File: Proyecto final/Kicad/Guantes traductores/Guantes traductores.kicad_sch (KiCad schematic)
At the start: 0 parts

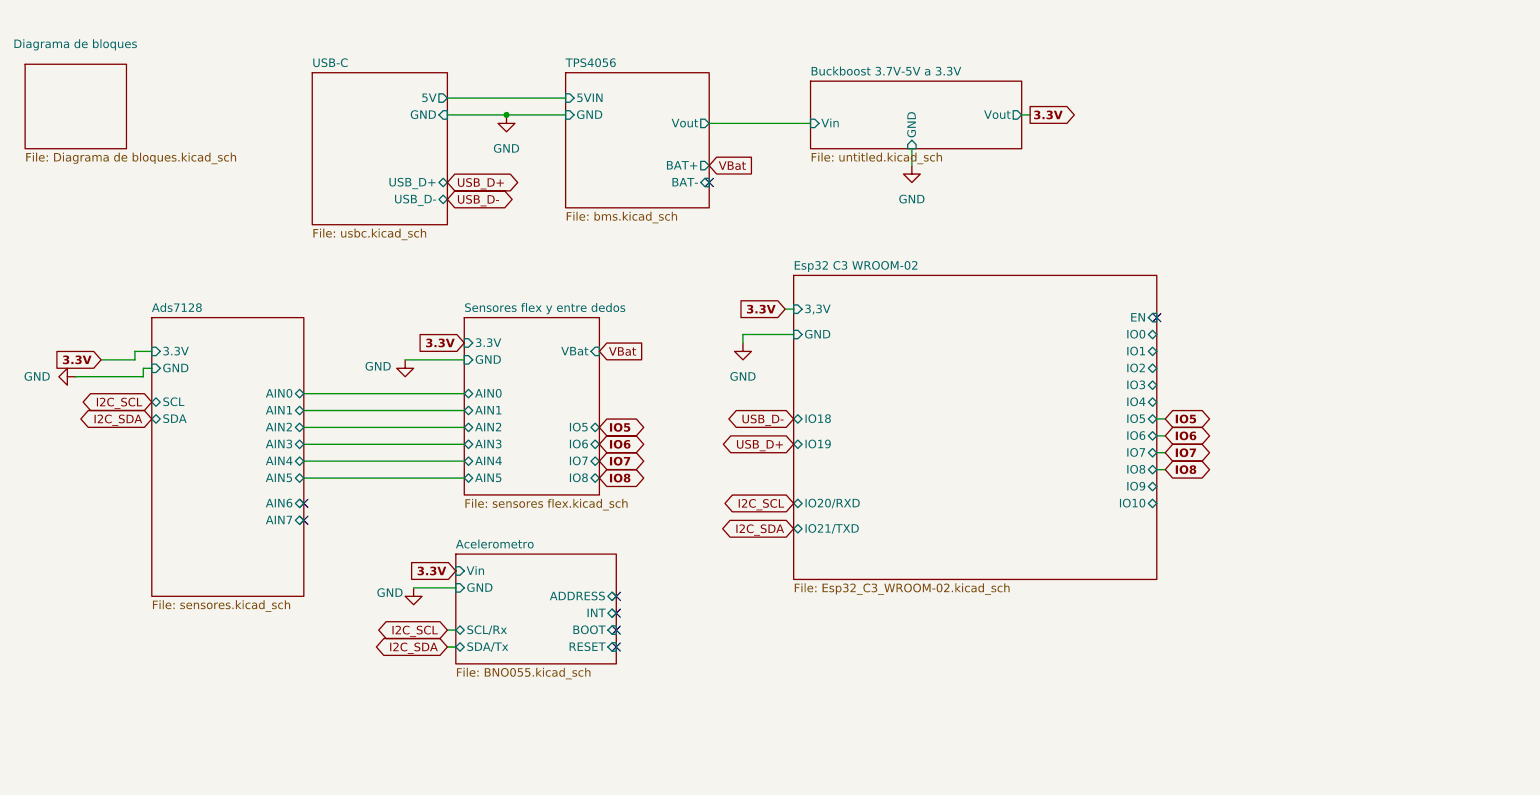
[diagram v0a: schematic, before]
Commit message: Posicion de componentes
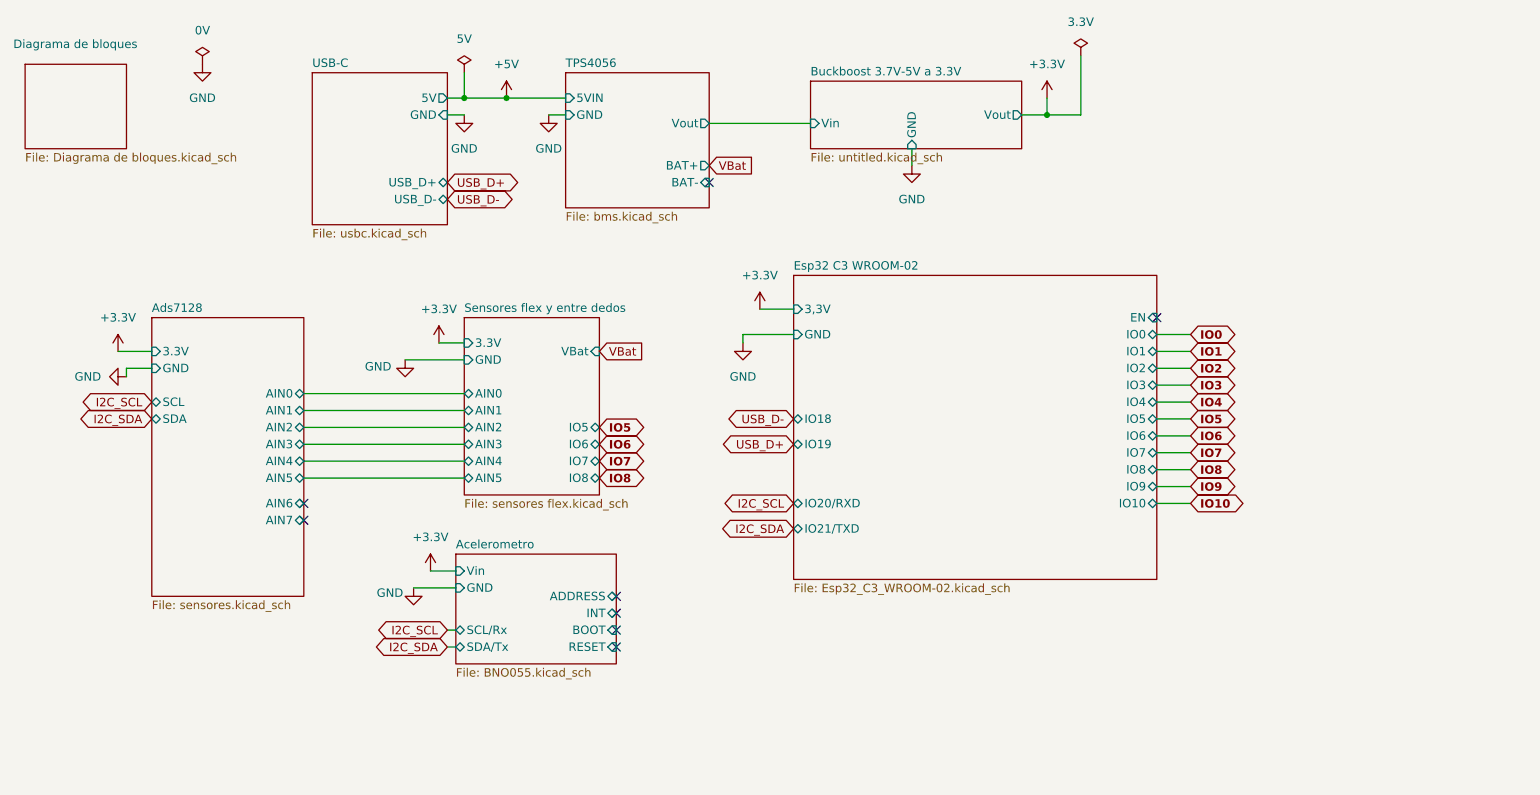
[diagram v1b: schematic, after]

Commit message: Avance de esquematicos
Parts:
- added R13, R21: 5.1k, Resistor_SMD:R_0805_2012Metric_Pad1.20x1.40mm_HandSolder, symbol Device:R
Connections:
- net +3.3V: now also R13.2, R21.2
- net I2C_SCL: now also R13.1
- net I2C_SDA: now also R21.1

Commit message: Avance enrutado pf
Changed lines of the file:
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@@
 	(wire
 		(pts
-			(xy 86.36 107.95) (xy 87.63 107.95)
+			(xy 81.28 107.95) (xy 87.63 107.95)
 		)
 		(stroke
@@
 	(wire
 		(pts
-			(xy 41.91 66.04) (xy 38.1 66.04)
+			(xy 41.91 66.04) (xy 31.75 66.04)
 		)
 		(stroke
@@
 	(wire
 		(pts
-			(xy 86.36 105.41) (xy 87.63 105.41)
+			(xy 81.28 105.41) (xy 87.63 105.41)
 		)
 		(stroke
@@
 		(pts
 			(xy 198.12 68.58) (xy 193.04 68.58)
-		)
-		(stroke
-			(width 0)
-			(type default)
-		)
-	)
-	(wire
-		(pts
-			(xy 38.1 66.04) (xy 38.1 67.31)
 		)
 		(stroke
@@
 	(global_label "I2C_SCL"
 		(shape bidirectional)
-		(at 86.36 105.41 180)
+		(at 81.28 105.41 180)
 		(fields_autoplaced yes)
 		(effects
@@
 		)
 		(property "Intersheetrefs" "${INTERSHEET_REFS}"
-			(at 74.704 105.41 0)
+			(at 69.624 105.41 0)
 			(hide yes)
 			(show_name no)
@@
 	(global_label "I2C_SDA"
 		(shape bidirectional)
-		(at 86.36 107.95 180)
+		(at 81.28 107.95 180)
 		(fields_autoplaced yes)
 		(effects
@@
 		)
 		(property "Intersheetrefs" "${INTERSHEET_REFS}"
-			(at 74.6435 107.95 0)
+			(at 69.5635 107.95 0)
 			(hide yes)
 			(show_name no)
@@
 	(symbol
 		(lib_id "power:GND")
-		(at 38.1 67.31 270)
+		(at 31.75 66.04 270)
 		(unit 1)
 		(body_style 1)
@@
 		(fields_autoplaced yes)
 		(property "Reference" "#PWR02"
-			(at 31.75 67.31 0)
+			(at 25.4 66.04 0)
 			(hide yes)
 			(show_name no)
@@
 		)
 		(property "Value" "GND"
-			(at 34.29 67.3099 90)
+			(at 27.94 66.0399 90)
 			(show_name no)
 			(do_not_autoplace no)
@@
 		)
 		(property "Footprint" ""
-			(at 38.1 67.31 0)
+			(at 31.75 66.04 0)
 			(hide yes)
 			(show_name no)
@@
 		)
 		(property "Datasheet" ""
-			(at 38.1 67.31 0)
+			(at 31.75 66.04 0)
 			(hide yes)
 			(show_name no)
@@
 		)
 		(property "Description" "Power symbol creates a global label with name \"GND\" , ground"
-			(at 38.1 67.31 0)
-			(hide yes)
-			(show_name no)
+			(at 31.75 66.04 0)
+			(hide yes)
+			(show_name no)

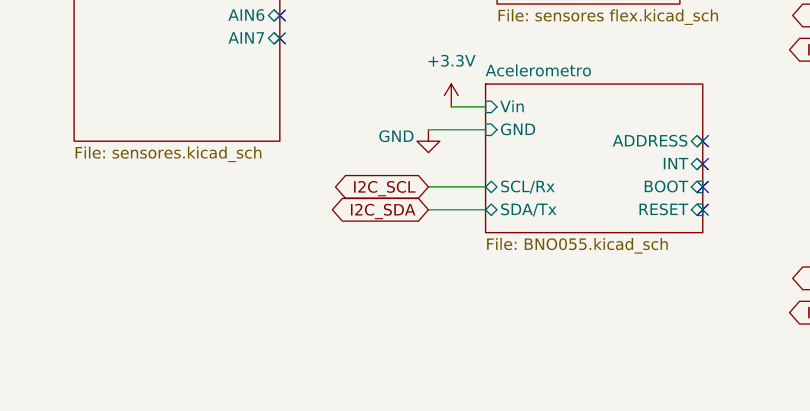
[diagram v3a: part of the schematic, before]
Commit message: Added TVS diodes in i2c channels
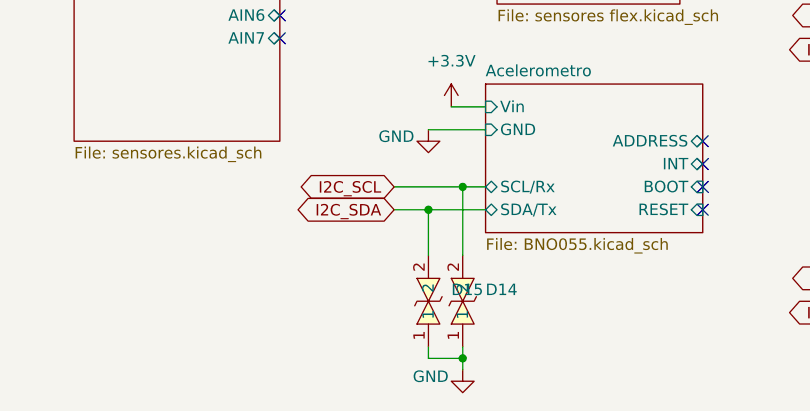
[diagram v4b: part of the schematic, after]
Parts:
- added D14, D15: ESD5B5.0ST1G, Diode_SMD:D_SOD-523, symbol ESD5B5.0ST1G:ESD5B5.0ST1G
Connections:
- net GND: now also D14.1, D15.1
- net I2C_SCL: now also D14.2
- net I2C_SDA: now also D15.2

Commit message: Switch y leds
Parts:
- added R28, R29: 200, Resistor_SMD:R_0805_2012Metric, symbol Device:R
- added U9: HSMF-C113_C6795902, lcsc_footprints:C6795902_LED-SMD_HSMF-C113, symbol lcsc_imported:HSMF-C113_C6795902
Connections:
- net +3.3V: now also U9.2
- net GND: now also R28.1
- net IO10: now also R29.1
- new net: R28.2, U9.3
- new net: R29.2, U9.4
- no-connect marks 8 -> 9
